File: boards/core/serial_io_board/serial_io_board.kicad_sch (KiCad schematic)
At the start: 36 parts, among them J1 Exp. Conn. A, J2 COM1, J2 Exp. Conn. B, J3 Power, J4 ~{RTS}/~{DTR} SELECT, J5 FTDI VCC SELECT, J6 FTDI, SW1 I/O Address / IRQ selection, SW2 FTDI_PT, U1 74LS04, U2 74LS139, U4 16550, U5 74LS688, U5 MAX232, X1 7.3728MHz

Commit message: * Working on new powerdistribution method.
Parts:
- removed CP3: 10uF, Capacitor_THT:CP_Radial_D5.0mm_P2.50mm, symbol Device:C_Polarized
- removed CP4: 0.1uF, Capacitor_THT:CP_Radial_D5.0mm_P2.50mm, symbol Device:C_Polarized
- removed J3: Power, Connector_IDC:IDC-Header_2x10_P2.54mm_Horizontal, symbol Connector_Generic:Conn_02x10_Top_Bottom
- removed J5: FTDI VCC SELECT, Connector_PinHeader_2.54mm:PinHeader_1x03_P2.54mm_Vertical, symbol Connector_Generic:Conn_01x03
- added J3: Power, footprints:TE_171826-4, symbol Connector_Generic:Conn_01x04
- R3: value 470 -> 1k
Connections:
- net SUPVCC is gone; now on net +5V: SW2.3
- net +5V: now also J3.4 (Pin_4)
- net GND: now also J3.2 (Pin_2), J3.3 (Pin_3)
- no-connect marks 89 -> 79

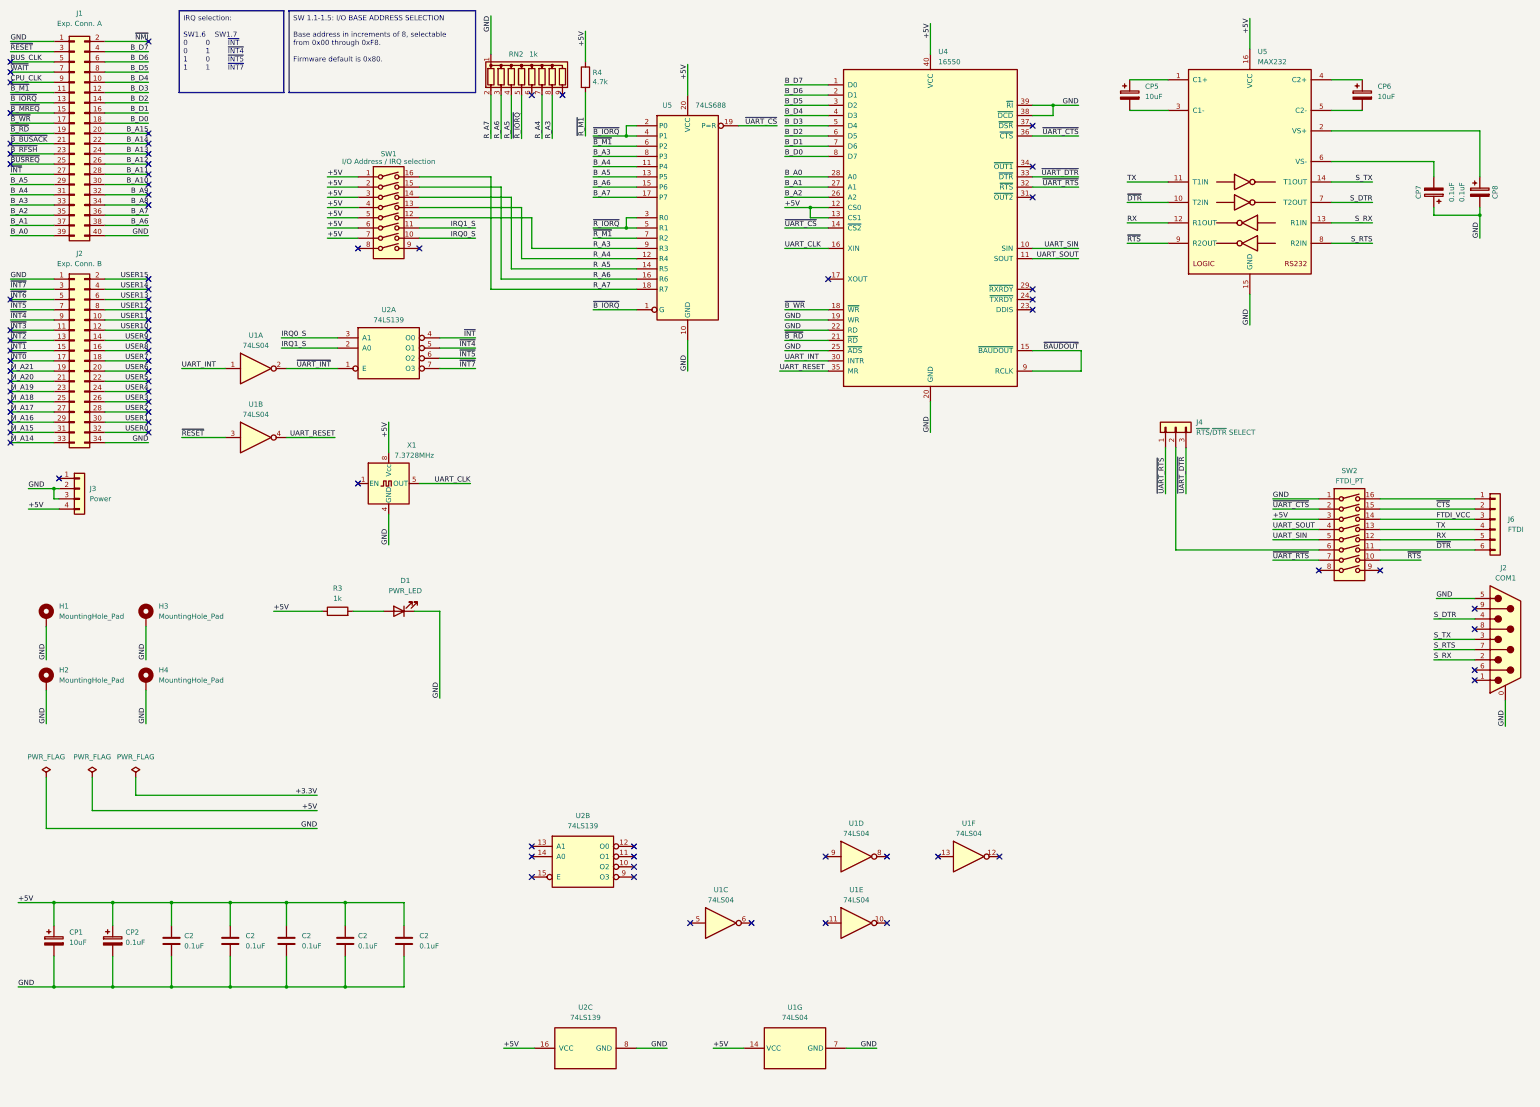
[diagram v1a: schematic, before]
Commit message: Added expansion connector C and designed some new boards around it.
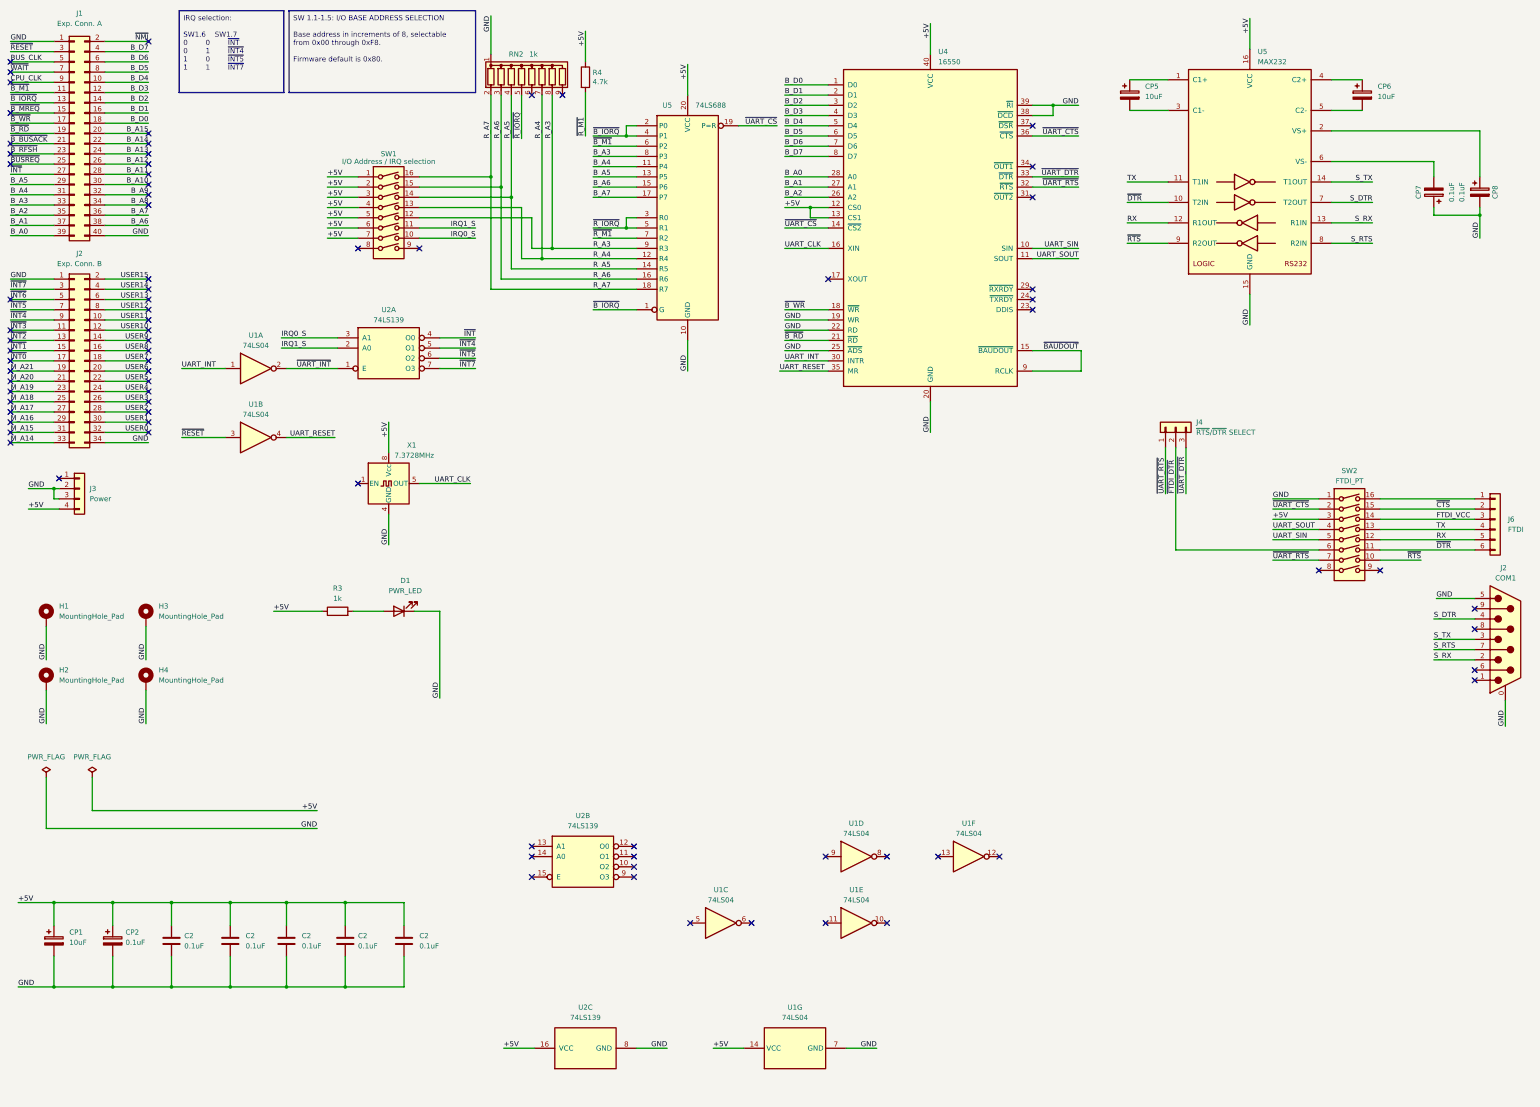
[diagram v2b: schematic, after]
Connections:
- net B_D0: now also U4.1 (D0); no longer U4.8 (D7)
- net B_D1: now also U4.2 (D1); no longer U4.7 (D6)
- net B_D2: now also U4.3 (D2); no longer U4.6 (D5)
- net B_D3: now also U4.4 (D3); no longer U4.5 (D4)
- net B_D4: now also U4.5 (D4); no longer U4.4 (D3)
- net B_D5: now also U4.6 (D5); no longer U4.3 (D2)
- net B_D6: now also U4.7 (D6); no longer U4.2 (D1)
- net B_D7: now also U4.8 (D7); no longer U4.1 (D0)
- net ~{FTDI_DTR}: now reaches J4.2 (Pin_2), SW2.6
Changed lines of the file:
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@@
   (title_block
     (title "Serial I/O board for the stackable Z80 computer")
-    (date "2023-10-23")
-    (rev "1.6")
+    (date "2024-02-19")
+    (rev "1.7")
   )
   (junction (at 27.305 256.54) (diameter 0) (color 0 0 0 0)
@@
   (junction (at 99.695 256.54) (diameter 0) (color 0 0 0 0)
   )
+  (junction (at 135.89 55.245) (diameter 0) (color 0 0 0 0)
+  )
   (junction (at 27.305 235.585) (diameter 0) (color 0 0 0 0)
   )
+  (junction (at 138.43 57.785) (diameter 0) (color 0 0 0 0)
+  )
   (junction (at 169.545 45.085) (diameter 0) (color 0 0 0 0)
   )
@@
   (junction (at 41.91 235.585) (diameter 0) (color 0 0 0 0)
   )
+  (junction (at 148.59 75.565) (diameter 0) (color 0 0 0 0)
+  )
   (junction (at 85.09 256.54) (diameter 0) (color 0 0 0 0)
   )
   (junction (at 27.305 132.715) (diameter 0) (color 0 0 0 0)
   )
+  (junction (at 151.13 73.025) (diameter 0) (color 0 0 0 0)
+  )
   (junction (at 71.12 235.585) (diameter 0) (color 0 0 0 0)
   )
   (junction (at 99.695 235.585) (diameter 0) (color 0 0 0 0)
+  )
+  (junction (at 140.97 60.325) (diameter 0) (color 0 0 0 0)
   )
   (junction (at 71.12 256.54) (diameter 0) (color 0 0 0 0)
@@
     (stroke (width 0) (type default))
   )
-  (wire (pts (xy 172.085 73.025) (xy 146.05 73.025))
+  (wire (pts (xy 172.085 73.025) (xy 151.13 73.025))
     (stroke (width 0) (type default))
   )
@@
     (stroke (width 0) (type default))
   )
+  (wire (pts (xy 151.13 73.025) (xy 146.05 73.025))
+    (stroke (width 0) (type default))
+  )
   (wire (pts (xy 16.51 69.85) (xy 27.305 69.85))
     (stroke (width 0) (type default))
@@
     (stroke (width 0) (type default))
   )
-  (wire (pts (xy 47.625 208.915) (xy 47.625 204.47))
-    (stroke (width 0) (type default))
-  )
   (wire (pts (xy 281.94 75.565) (xy 270.51 75.565))
     (stroke (width 0) (type default))
@@
     (stroke (width 0) (type default))
   )
-  (wire (pts (xy 151.13 45.72) (xy 151.13 34.925))
+  (wire (pts (xy 151.13 34.925) (xy 151.13 73.025))
     (stroke (width 0) (type default))
   )
@@
     (stroke (width 0) (type default))
   )
+  (wire (pts (xy 148.59 75.565) (xy 143.51 75.565))
+    (stroke (width 0) (type default))
+  )
   (wire (pts (xy 208.915 62.865) (xy 215.265 62.865))
     (stroke (width 0) (type default))
@@
     (stroke (width 0) (type default))
   )
+  (wire (pts (xy 138.43 34.925) (xy 138.43 57.785))
+    (stroke (width 0) (type default))
+  )
   (wire (pts (xy 172.085 78.105) (xy 140.97 78.105))
     (stroke (width 0) (type default))
@@
     (stroke (width 0) (type default))
   )
-  (wire (pts (xy 148.59 45.72) (xy 148.59 34.925))
+  (wire (pts (xy 148.59 34.925) (xy 148.59 75.565))
     (stroke (width 0) (type default))
   )
@@
     (stroke (width 0) (type default))
   )
-  (wire (pts (xy 172.085 75.565) (xy 143.51 75.565))
+  (wire (pts (xy 172.085 75.565) (xy 148.59 75.565))
     (stroke (width 0) (type default))
   )
@@
     (stroke (width 0) (type default))
   )
-  (wire (pts (xy 138.43 45.72) (xy 138.43 34.925))
-    (stroke (width 0) (type default))
-  )
   (wire (pts (xy 135.89 55.245) (xy 135.89 83.185))
     (stroke (width 0) (type default))
@@
     (stroke (width 0) (type default))
   )
-  (wire (pts (xy 140.97 45.72) (xy 140.97 34.925))
+  (wire (pts (xy 140.97 34.925) (xy 140.97 60.325))
     (stroke (width 0) (type default))
   )
@@
     (stroke (width 0) (type default))
   )
-  (wire (pts (xy 92.71 208.915) (xy 47.625 208.915))
-    (stroke (width 0) (type default))
-  )
   (wire (pts (xy 50.8 29.21) (xy 40.005 29.21))
     (stroke (width 0) (type default))
@@
     (stroke (width 0) (type default))
   )
+  (wire (pts (xy 135.89 34.925) (xy 135.89 55.245))
+    (stroke (width 0) (type default))
+  )
   (wire (pts (xy 370.205 51.435) (xy 370.205 55.245))
     (stroke (width 0) (type default))
@@
   )
   (wire (pts (xy 132.08 95.25) (xy 123.19 95.25))
-    (stroke (width 0) (type default))
-  )
-  (wire (pts (xy 135.89 45.72) (xy 135.89 34.925))
     (stroke (width 0) (type default))
   )
@@
     (effects (font (size 1.27 1.27)) (justify right bottom))
   )
-  (label "B_D5" (at 208.915 37.465 0) (fields_autoplaced)
+  (label "B_D5" (at 208.915 45.085 0) (fields_autoplaced)
     (effects (font (size 1.27 1.27)) (justify left bottom))
   )
@@
     (effects (font (size 1.27 1.27)) (justify left bottom))
   )
-  (label "B_D4" (at 208.915 40.005 0) (fields_autoplaced)
+  (label "B_D4" (at 208.915 42.545 0) (fields_autoplaced)
     (effects (font (size 1.27 1.27)) (justify left bottom))
   )
@@
     (effects (font (size 1.27 1.27)) (justify right bottom))
   )
-  (label "B_D0" (at 208.915 50.165 0) (fields_autoplaced)
+  (label "B_D0" (at 208.915 32.385 0) (fields_autoplaced)
     (effects (font (size 1.27 1.27)) (justify left bottom))
   )
@@
     (effects (font (size 1.27 1.27)) (justify left bottom))
   )
-  (label "B_D1" (at 208.915 47.625 0) (fields_autoplaced)
+  (label "B_D1" (at 208.915 34.925 0) (fields_autoplaced)
     (effects (font (size 1.27 1.27)) (justify left bottom))
   )
@@
     (effects (font (size 1.27 1.27)) (justify left bottom))
   )
-  (label "B_D7" (at 208.915 32.385 0) (fields_autoplaced)
+  (label "B_D7" (at 208.915 50.165 0) (fields_autoplaced)
     (effects (font (size 1.27 1.27)) (justify left bottom))
   )
@@
     (effects (font (size 1.27 1.27)) (justify right bottom))
   )
-  (label "B_D6" (at 208.915 34.925 0) (fields_autoplaced)
+  (label "~{FTDI_DTR}" (at 306.07 133.985 90) (fields_autoplaced)
+    (effects (font (size 1.27 1.27)) (justify left bottom))
+  )
+  (label "B_D6" (at 208.915 47.625 0) (fields_autoplaced)
     (effects (font (size 1.27 1.27)) (justify left bottom))
   )
@@
     (effects (font (size 1.27 1.27)) (justify left bottom))
   )
-  (label "B_D2" (at 208.915 45.085 0) (fields_autoplaced)
+  (label "B_D2" (at 208.915 37.465 0) (fields_autoplaced)
     (effects (font (size 1.27 1.27)) (justify left bottom))
   )
@@
     (effects (font (size 1.27 1.27)) (justify right bottom))
   )
-  (label "B_D3" (at 208.915 42.545 0) (fields_autoplaced)
+  (label "B_D3" (at 208.915 40.005 0) (fields_autoplaced)
     (effects (font (size 1.27 1.27)) (justify left bottom))
   )
@@
   )
   (label "UART_SOUT" (at 281.94 75.565 180) (fields_autoplaced)
-    (effects (font (size 1.27 1.27)) (justify right bottom))
-  )
-  (label "+3.3V" (at 92.71 208.915 180) (fields_autoplaced)
     (effects (font (size 1.27 1.27)) (justify right bottom))
   )
@@
         )
       )
-    )
-  )
-  (symbol (lib_id "power:PWR_FLAG") (at 47.625 204.47 0) (unit 1)
-    (in_bom yes) (on_board yes) (dnp no) (fields_autoplaced)
-    (property "Reference" "#FLG05" (at 47.625 202.565 0)
-      (effects (font (size 1.27 1.27)) hide)
-    )
-    (property "Value" "PWR_FLAG" (at 47.625 199.39 0)
-      (effects (font (size 1.27 1.27)))
-    )
-    (property "Footprint" "" (at 47.625 204.47 0)
-      (effects (font (size 1.27 1.27)) hide)
-    )
-    (property "Datasheet" "~" (at 47.625 204.47 0)
-      (effects (font (size 1.27 1.27)) hide)
-    )
-    (pin "1")
-    (instances
-      (project "backplane"
-        (path "/646a2674-5a23-45dc-998f-75b30368ef1d/d9bf800e-45bc-440e-a87f-31a60f80b1c6"
-          (reference "#FLG05") (unit 1)
-        )
-      )
-      (project "serial_io_board"
-        (path "/bddfa220-0b4a-4a31-8ec9-ee6ca5aa59a1"
-          (reference "#FLG03") (unit 1)
-        )
-      )

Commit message: Preparation for assembly order with PCBWay
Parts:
- C2: MPN (none) -> FG28X7R1H104KNT06; Manufacturer (none) -> TDK; Package (none) -> Plugin,P=5mm
- CP1, CP5, CP6: MPN (none) -> ECA1HM100I; Manufacturer (none) -> PANASONIC; Package (none) -> Plugin,D5xL11mm
- CP2, CP7, CP8: MPN (none) -> KS104M050C07RR0VH2FP0; Manufacturer (none) -> CX(Dongguan Chengxing Elec); Package (none) -> Plugin,D4xL7mm
- D1: MPN (none) -> HLMP-1700; Manufacturer (none) -> Broadcom/AVAGO; Package (none) -> LED_D3.0mm
- H1, H2, H3, H4: now left out of the parts list
- J1: MPN (none) -> X9555WR-2x20-6TV01; Manufacturer (none) -> XKB Connectivity; Package (none) -> Push-Pull,P=2.54mm
- J2: MPN (none) -> 5747840-4; Manufacturer (none) -> TE Connectivity; Package (none) -> Push-Pull
- J2: MPN (none) -> X9555WR-2x17-6TV01; Manufacturer (none) -> XKB Connectivity; Package (none) -> Push-Pull,P=2.54mm
- J3: MPN (none) -> 171826-4; Manufacturer (none) -> TE Connectivity AMP Connectors; Package (none) -> Plugin
- J4: MPN (none) -> 5-146277-3; Manufacturer (none) -> TE Connectivity; Package (none) -> Push-Pull,P=2.54mm
- J6: MPN (none) -> PPPC061LGBN-RC; Manufacturer (none) -> Sullins Connector Solutions; Package (none) -> Plugin,P=2.54mm
- R3: MPN (none) -> MFR2WSFTE73-1K; Manufacturer (none) -> YAGEO; Package (none) -> Plugin
- R4: MPN (none) -> MF0207FTE52-4K7; Manufacturer (none) -> YAGEO; Package (none) -> Plugin
- RN2: MPN (none) -> A09-472JP; Manufacturer (none) -> FH (Guangdong Fenghua Advanced Tech); Package (none) -> SIP-9-2.54mm
- SW1, SW2: MPN (none) -> DS-08BLP; Manufacturer (none) -> XKB Connection; Package (none) -> Plugin
- U1: MPN (none) -> 1-2199298-3; Manufacturer (none) -> TE Connectivity; Package (none) -> Plugin
- U2, U5: MPN (none) -> 1-2199298-4; Manufacturer (none) -> TE Connectivity; Package (none) -> Plugin
- U4: MPN (none) -> 1-2199299-5; Manufacturer (none) -> TE Connectivity; Package (none) -> Plugin
- U5: MPN (none) -> 1-2199298-6; Manufacturer (none) -> TE Connectivity; Package (none) -> Plugin
- X1: MPN (none) -> 1-2199298-2; Manufacturer (none) -> TE Connectivity; Package (none) -> Plugin

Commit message: Updated serial I/O board last weekend.
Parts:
- SW1: value I/O Address / IRQ selection -> I/O Address / IRQ select
- renumbered J2 to J?
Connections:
- net +5V: now also U2.15 (E)
- net GND: now also U2.13 (A1), U2.14 (A0)
- net IRQ0_S: now also SW1.11, U2.2 (A0); no longer SW1.10, U2.3 (A1)
- net IRQ1_S: now also SW1.10, U2.3 (A1); no longer SW1.11, U2.2 (A0)
- net R_A3: now also SW1.16; no longer SW1.12
- net R_A4: now also SW1.15; no longer SW1.13
- net R_A6: now also SW1.13; no longer SW1.15
- net R_A7: now also SW1.12; no longer SW1.16
- no-connect marks 79 -> 76
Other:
- moved on the sheet: C2, CP1, CP5, CP6, CP7, CP8, D1, H1, H3, H4, J1, J2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
